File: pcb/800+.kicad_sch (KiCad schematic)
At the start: 35 parts, among them J1 2inch LCD, J6 ESP_JTAG, J7 ESP_PROG, Q1 AO3401A, Q2 AO3401A, Q3 AO3401A, Q4 AO3401A, U12 VEML7700-TR, U2 ESP32-S3-WROOM-1U, U7 TSOP75340TT

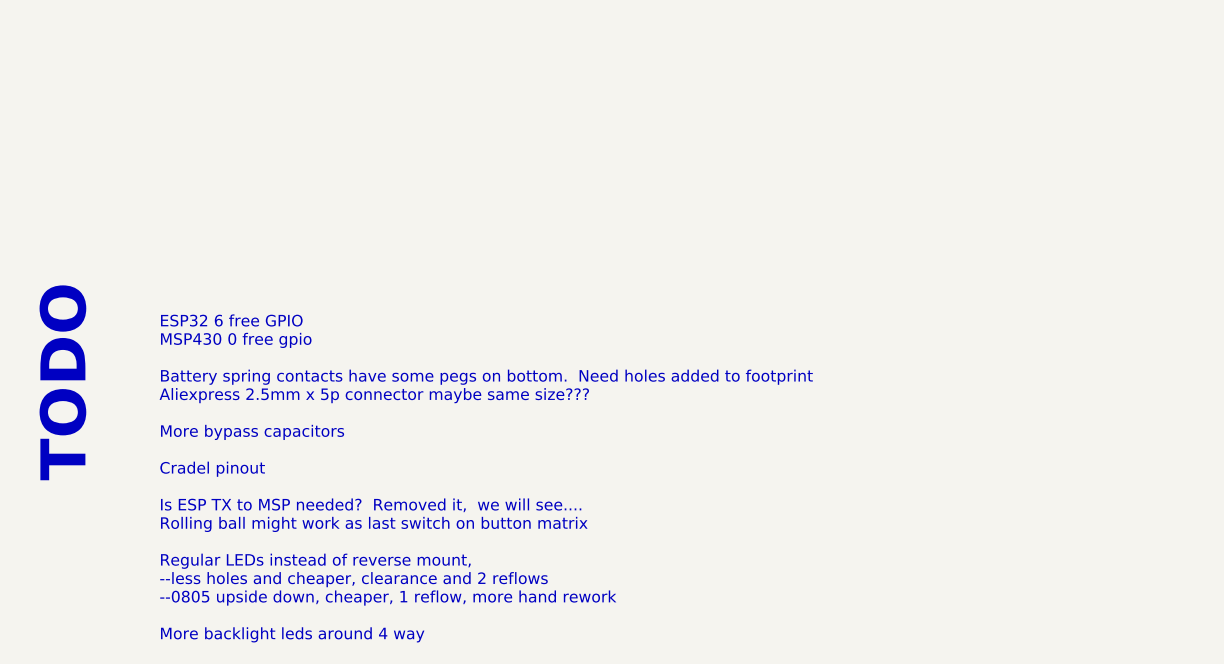
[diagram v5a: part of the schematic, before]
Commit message: fix battery connector
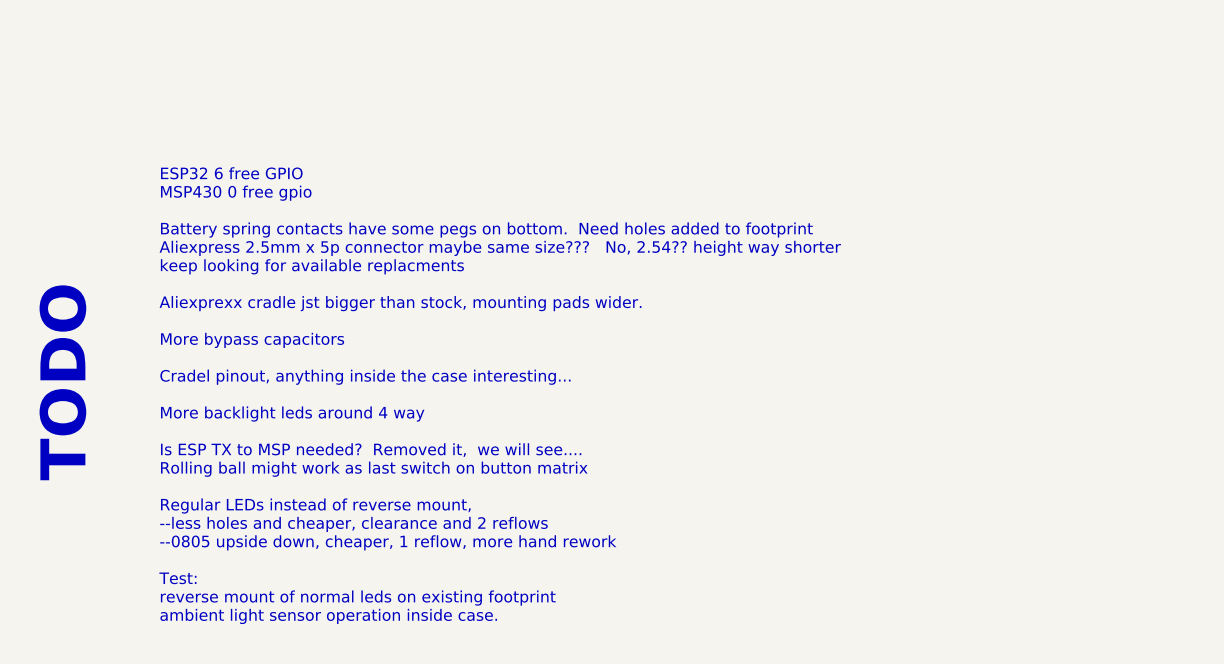
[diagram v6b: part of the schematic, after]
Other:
- note added: "ESP32 6 free GPIO MSP430 0 free gpio Battery spring contacts have some pegs on bottom. Need holes added to footprint Aliexpress 2.5mm x 5p connector maybe same size??? No, 2.54?? height way shorter keep looking for available replacments Aliexprexx cradle jst bigger than stock, mounting pads wider. More bypass capacitors Cradel pinout, anything inside the case interesting... More backlight leds ar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"
- note removed: "ESP32 6 free GPIO MSP430 0 free gpio Battery spring contacts have some pegs on bottom. Need holes added to footprint Aliexpress 2.5mm x 5p connector maybe same size??? More bypass capacitors Cradel pinout Is ESP TX to MSP needed? Removed it, we will see.... Rolling ball might work as last switch on button matrix Regular LEDs instead of reverse mount, --less holes and cheaper, clearance and 2 refl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"
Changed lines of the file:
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@@
     (effects (font (size 1.27 1.27)) (justify left bottom))
   )
-  (text "ESP32 6 free GPIO\nMSP430 0 free gpio\n\nBattery spring contacts have some pegs on bottom.  Need holes added to footprint\nAliexpress 2.5mm x 5p connector maybe same size???\n\nMore bypass capacitors\n\nCradel pinout\n\nIs ESP TX to MSP needed?  Removed it,  we will see....\nRolling ball might work as last switch on button matrix\n\nRegular LEDs instead of reverse mount, \n--less holes and cheaper, clearance and 2 reflows\n--0805 upside down, cheaper, 1 reflow, more hand rework\n\nMore backlight leds around 4 way"
+  (text "ESP32 6 free GPIO\nMSP430 0 free gpio\n\nBattery spring contacts have some pegs on bottom.  Need holes added to footprint\nAliexpress 2.5mm x 5p connector maybe same size???   No, 2.54?? height way shorter\nkeep looking for available replacments\n\nAliexprexx cradle jst bigger than stock, mounting pads wider.\n\nMore bypass capacitors\n\nCradel pinout, anything inside the case interesting...\n\nMore backlight leds around 4 way\n\nIs ESP TX to MSP needed?  Removed it,  we will see....\nRolling ball might work as last switch on button matrix\n\nRegular LEDs instead of reverse mount, \n--less holes and cheaper, clearance and 2 reflows\n--0805 upside down, cheaper, 1 reflow, more hand rework\n\nTest:\nreverse mount of normal leds on existing footprint\nambient light sensor operation inside case.\n\n"
     (at 35.56 267.97 0)
     (effects (font (size 1.27 1.27)) (justify left bottom))
@@
       (effects (font (size 1.27 1.27)) (justify left top) hide)
     )
-    (pin "2")
-    (pin "1")
+    (pin "1")
+    (pin "2")
     (pin "3")
     (pin "4")
@@
     )
     (pin "1")
+    (pin "2")
     (pin "3")
-    (pin "2")
     (instances
       (project "800+"
@@
       (effects (font (size 1.27 1.27)) hide)
     )
-    (pin "2")
-    (pin "1")
-    (instances
-      (project "800+"
+    (pin "1")
+    (pin "2")
+    (instances
+      (project "800+"

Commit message: cradle connector
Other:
- note added: "ESP32 6 free GPIO MSP430 0 free gpio Aliexpress 2.5mm x 5p connector fits battery snuggly, too short keep looking for available replacments Aliexprexx cradle jst bigger than stock, mounting pads wider. Maybe not jst, molex or amphenol? More bypass capacitors battery thermistor, find way to pulse or control supply current vref from msp430, one of the port 2 inputs switched briefly. More backlight 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"
- note removed: "ESP32 6 free GPIO MSP430 0 free gpio Battery spring contacts have some pegs on bottom. Need holes added to footprint Aliexpress 2.5mm x 5p connector maybe same size??? No, 2.54?? height way shorter keep looking for available replacments Aliexprexx cradle jst bigger than stock, mounting pads wider. More bypass capacitors Cradel pinout, anything inside the case interesting... More backlight leds ar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"
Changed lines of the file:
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@@
     (effects (font (size 1.27 1.27)) (justify left bottom))
   )
-  (text "ESP32 6 free GPIO\nMSP430 0 free gpio\n\nBattery spring contacts have some pegs on bottom.  Need holes added to footprint\nAliexpress 2.5mm x 5p connector maybe same size???   No, 2.54?? height way shorter\nkeep looking for available replacments\n\nAliexprexx cradle jst bigger than stock, mounting pads wider.\n\nMore bypass capacitors\n\nCradel pinout, anything inside the case interesting...\n\nMore backlight leds around 4 way\n\nIs ESP TX to MSP needed?  Removed it,  we will see....\nRolling ball might work as last switch on button matrix\n\nRegular LEDs instead of reverse mount, \n--less holes and cheaper, clearance and 2 reflows\n--0805 upside down, cheaper, 1 reflow, more hand rework\n\nTest:\nreverse mount of normal leds on existing footprint\nambient light sensor operation inside case.\n\n"
+  (text "ESP32 6 free GPIO\nMSP430 0 free gpio\n\nAliexpress 2.5mm x 5p connector fits battery snuggly, too short\nkeep looking for available replacments\n\nAliexprexx cradle jst bigger than stock, mounting pads wider.\nMaybe not jst, molex or amphenol?\n\nMore bypass capacitors\n\nbattery thermistor, find way to pulse or control supply current\nvref from msp430, one of the port 2 inputs switched briefly.\n\nMore backlight leds around 4 way\n\nIs ESP TX to MSP needed?  Removed it,  we will see....\nRolling ball might work as last switch on button matrix\n\nRegular LEDs instead of reverse mount, \n--less holes and cheaper, clearance and 2 reflows\n--1206 upside down, cheaper, 1 reflow, more hand rework\n\nTest:\nreverse mount of normal leds on existing footprint, 0805 too small\nambient light sensor operation inside case.\n\n"
     (at 35.56 267.97 0)
     (effects (font (size 1.27 1.27)) (justify left bottom))

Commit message: parts placed
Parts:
- added C9: 1u, Capacitor_SMD:C_0805_2012Metric, symbol Device:C
- renumbered D33 to IR1, D34 to IR2
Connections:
- net +3.3VP: now also C9.1
- net GND: now also C9.2
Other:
- note added: "ESP32 6 free GPIO MSP430 0 free gpio Aliexpress 2.5mm x 5p connector fits battery snuggly, too short keep looking for available replacments Aliexprexx cradle jst bigger than stock, mounting pads wider. Plug fits, update footprint Maybe not jst, molex or amphenol? battery thermistor, find way to pulse or control supply current vref from msp430, one of the port 2 inputs switched briefly. Is ESP TX 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"
- note removed: "ESP32 6 free GPIO MSP430 0 free gpio Aliexpress 2.5mm x 5p connector fits battery snuggly, too short keep looking for available replacments Aliexprexx cradle jst bigger than stock, mounting pads wider. Maybe not jst, molex or amphenol? More bypass capacitors battery thermistor, find way to pulse or control supply current vref from msp430, one of the port 2 inputs switched briefly. More backlight 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"
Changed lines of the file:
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@@
   (junction (at 245.11 37.465) (diameter 0) (color 0 0 0 0)
   )
+  (junction (at 49.53 25.4) (diameter 0) (color 0 0 0 0)
+  )
   (junction (at 245.11 45.085) (diameter 0) (color 0 0 0 0)
   )
@@
   (junction (at 26.035 113.03) (diameter 0) (color 0 0 0 0)
   )
+  (junction (at 49.53 35.56) (diameter 0) (color 0 0 0 0)
+  )
   (junction (at 102.235 38.1) (diameter 0) (color 0 0 0 0)
   )
@@
     (stroke (width 0) (type default))
   )
+  (wire (pts (xy 49.53 25.4) (xy 49.53 26.67))
+    (stroke (width 0) (type default))
+  )
   (wire (pts (xy 148.59 138.43) (xy 163.83 138.43))
     (stroke (width 0) (type default))
@@
     (stroke (width 0) (type default))
   )
+  (wire (pts (xy 49.53 34.29) (xy 49.53 35.56))
+    (stroke (width 0) (type default))
+  )
   (wire (pts (xy 79.375 66.675) (xy 67.945 66.675))
     (stroke (width 0) (type default))
@@
     (stroke (width 0) (type default))
   )
-  (wire (pts (xy 47.625 25.4) (xy 55.245 25.4))
+  (wire (pts (xy 47.625 25.4) (xy 49.53 25.4))
     (stroke (width 0) (type default))
   )
@@
     (stroke (width 0) (type default))
   )
+  (wire (pts (xy 49.53 25.4) (xy 55.245 25.4))
+    (stroke (width 0) (type default))
+  )
   (wire (pts (xy 224.155 125.73) (xy 247.015 125.73))
     (stroke (width 0) (type default))
@@
     (stroke (width 0) (type default))
   )
-  (wire (pts (xy 47.625 35.56) (xy 55.245 35.56))
+  (wire (pts (xy 47.625 35.56) (xy 49.53 35.56))
     (stroke (width 0) (type default))
   )
@@
     (stroke (width 0) (type default))
   )
+  (wire (pts (xy 49.53 35.56) (xy 55.245 35.56))
+    (stroke (width 0) (type default))
+  )
   (wire (pts (xy 148.59 143.51) (xy 162.56 143.51))
     (stroke (width 0) (type default))
@@
     (effects (font (size 1.27 1.27)) (justify left bottom))
   )
-  (text "ESP32 6 free GPIO\nMSP430 0 free gpio\n\nAliexpress 2.5mm x 5p connector fits battery snuggly, too short\nkeep looking for available replacments\n\nAliexprexx cradle jst bigger than stock, mounting pads wider.\nMaybe not jst, molex or amphenol?\n\nMore bypass capacitors\n\nbattery thermistor, find way to pulse or control supply current\nvref from msp430, one of the port 2 inputs switched briefly.\n\nMore backlight leds around 4 way\n\nIs ESP TX to MSP needed?  Removed it,  we will see....\nRolling ball might work as last switch on button matrix\n\nRegular LEDs instead of reverse mount, \n--less holes and cheaper, clearance and 2 reflows\n--1206 upside down, cheaper, 1 reflow, more hand rework\n\nTest:\nreverse mount of normal leds on existing footprint, 0805 too small\nambient light sensor operation inside case.\n\n"
-    (at 35.56 267.97 0)
+  (text "ESP32 6 free GPIO\nMSP430 0 free gpio\n\nAliexpress 2.5mm x 5p connector fits battery snuggly, too short\nkeep looking for available replacments\n\nAliexprexx cradle jst bigger than stock, mounting pads wider.\nPlug fits, update footprint\nMaybe not jst, molex or amphenol?\n\nbattery thermistor, find way to pulse or control supply current\nvref from msp430, one of the port 2 inputs switched briefly.\n\nIs ESP TX to MSP needed?  Removed it,  we will see....\nRolling ball might work as last switch on button matrix\n\nRegular LEDs instead of reverse mount, \n--less holes and cheaper, clearance and 2 reflows.  Tape to mount switch domes more complicated\n--1206 upside down, cheaper, 1 reflow, more hand rework\n--SK6812Mini reverse mount, cheap,  but bigger cutout battery compartment clearance\n\nTest:\nambient light sensor operation inside case.\n\n"
+    (at 29.21 274.32 0)
     (effects (font (size 1.27 1.27)) (justify left bottom))
   )
@@
   (symbol (lib_id "Device:LED") (at 142.875 50.8 180) (unit 1)
     (in_bom yes) (on_board yes) (dnp no) (fields_autoplaced)
-    (property "Reference" "D33" (at 144.4625 43.815 0)
+    (property "Reference" "IR1" (at 144.4625 44.45 0)
       (effects (font (size 1.27 1.27)))
     )
-    (property "Value" "LED" (at 144.4625 46.355 0)
+    (property "Value" "LED" (at 144.4625 46.99 0)
       (effects (font (size 1.27 1.27)))
     )
@@
       (project "800+"
         (path "/e63e39d7-6ac0-4ffd-8aa3-1841a4541b55"
-          (reference "D33") (unit 1)
+          (reference "IR1") (unit 1)
+        )
+      )
+    )
+  )
+  (symbol (lib_id "Device:C") (at 49.53 30.48 0) (unit 1)
+    (in_bom yes) (on_board yes) (dnp no)
+    (property "Reference" "C9" (at 50.165 27.94 0)
+      (effects (font (size 1.27 1.27)) (justify left))
+    )
+    (property "Value" "1u" (at 50.165 33.02 0)
+      (effects (font (size 1.27 1.27)) (justify left))
+    )
+    (property "Footprint" "Capacitor_SMD:C_0805_2012Metric" (at 50.4952 34.29 0)
+      (effects (font (size 1.27 1.27)) hide)
+    )
+    (property "Datasheet" "" (at 49.53 30.48 0)
+      (effects (font (size 1.27 1.27)))
+    )
+    (pin "1")
+    (pin "2")
+    (instances
+      (project "Random_SRAM"
+        (path "/6a282786-96e2-4c0a-ad5f-81da2c34d34d"
+          (reference "C9") (unit 1)
+        )
+      )
+      (project "800+"
+        (path "/e63e39d7-6ac0-4ffd-8aa3-1841a4541b55"
+          (reference "C17") (unit 1)
         )
       )
@@
   (symbol (lib_id "Device:LED") (at 142.875 58.42 180) (unit 1)
     (in_bom yes) (on_board yes) (dnp no)
-    (property "Reference" "D34" (at 142.875 61.595 0)
+    (property "Reference" "IR2" (at 142.875 61.595 0)
       (effects (font (size 1.27 1.27)))
     )
@@
       (project "800+"
         (path "/e63e39d7-6ac0-4ffd-8aa3-1841a4541b55"
-          (reference "D34") (unit 1)
+          (reference "IR2") (unit 1)
         )
       )
